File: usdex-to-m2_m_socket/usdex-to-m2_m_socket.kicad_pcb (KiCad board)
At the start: 6 copper layers, 44 x 39.4 mm, 10 parts, among them J1 Conn_02x01, J2 Bus_M.2_Socket_M, J3 Conn_01x02_Pin, J4 Micro_SDex_PCB, J5 Conn_01x02_Pin, J6 Conn_01x02_Pin, J7 Conn_01x10_Pin

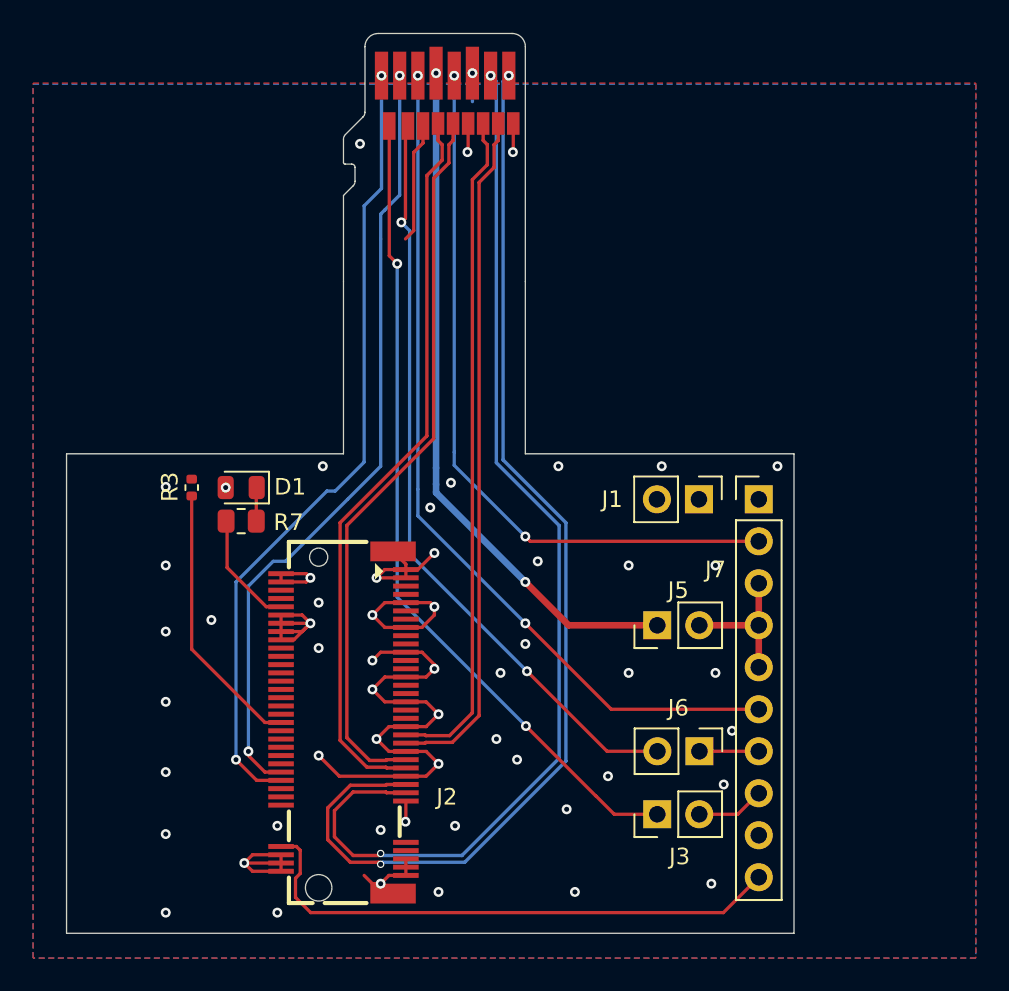
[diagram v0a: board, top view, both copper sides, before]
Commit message: usdex-to-m2_m_socket: fillet tracks
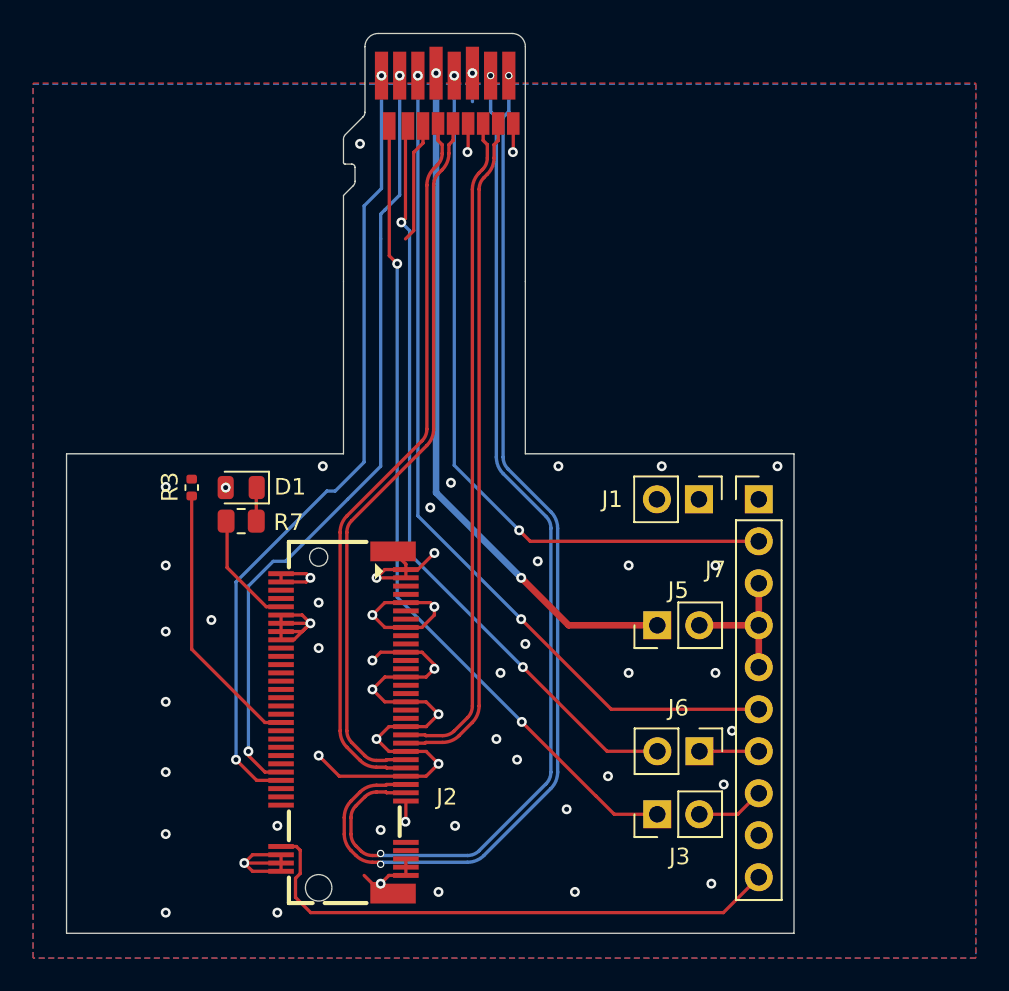
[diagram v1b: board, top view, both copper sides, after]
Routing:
- net DATx/REFCLK-: track 68.0 -> 65.7 mm
- net DATx/REFCLK+: track 66.0 -> 63.8 mm

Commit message: usdex-to-m2_m_socket: tune skew
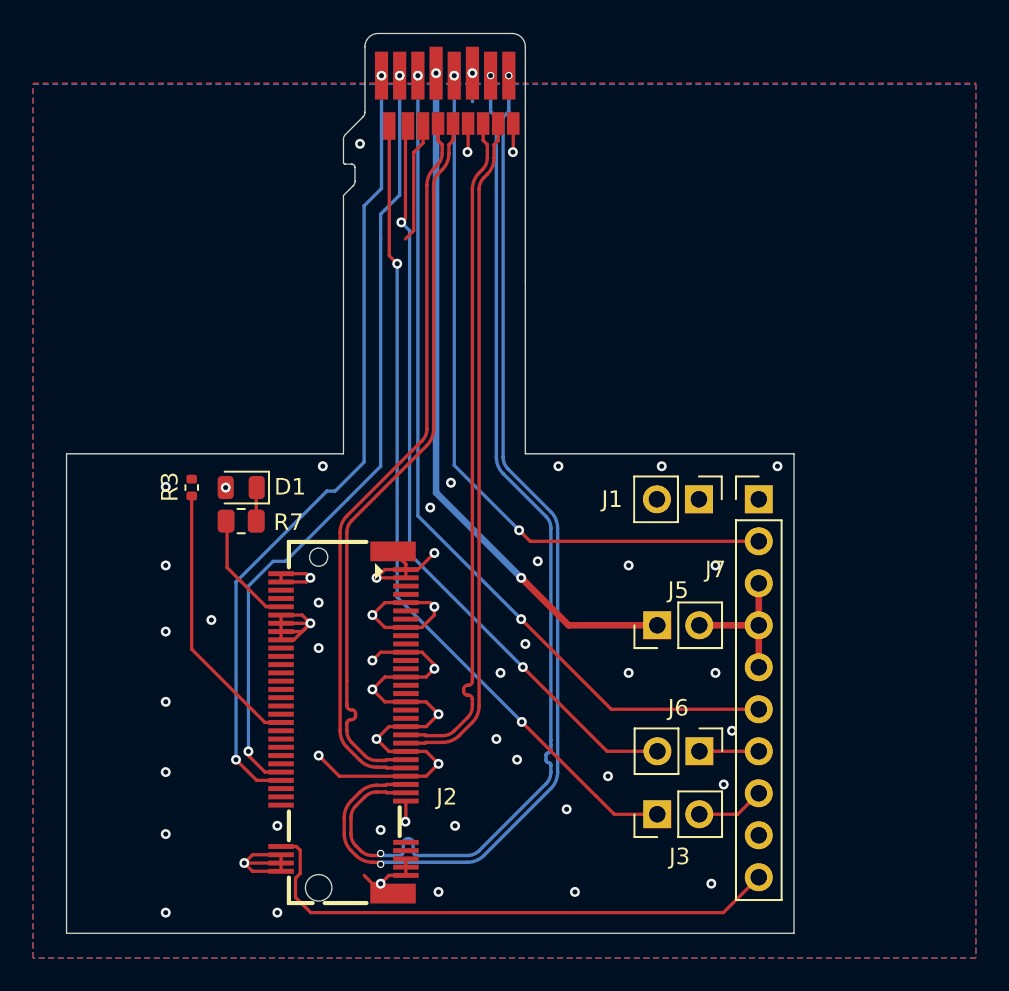
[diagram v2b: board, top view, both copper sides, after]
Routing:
- net DATx/REFCLK+: track 63.8 -> 65.6 mm
- net PCIe_TX-: track 43.6 -> 44.2 mm
- net PCIe_RX-: track 40.5 -> 41.1 mm

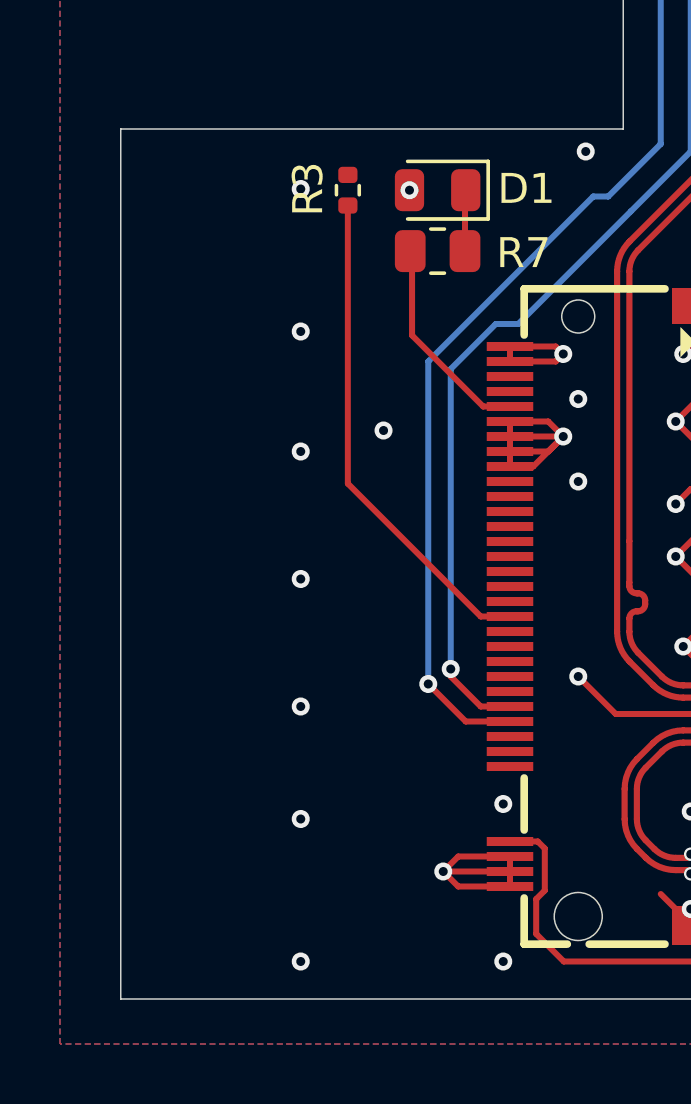
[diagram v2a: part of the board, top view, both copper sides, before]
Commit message: usdex-to-m2_m_socket: move GND vias
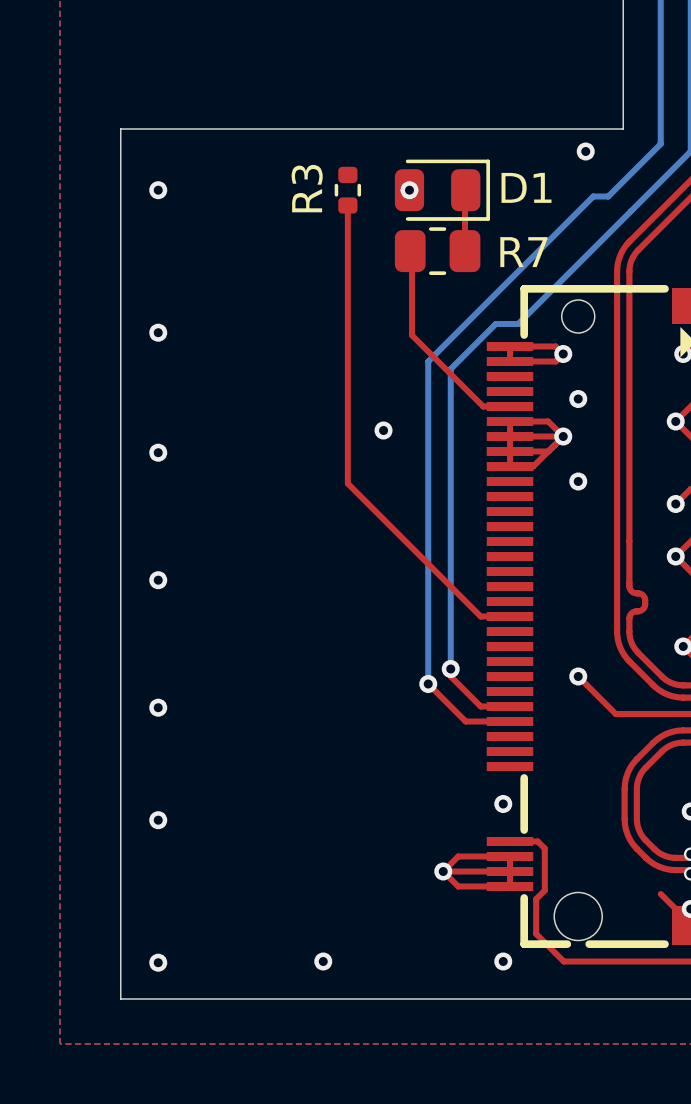
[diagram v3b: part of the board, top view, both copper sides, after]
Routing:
- net GND: vias 53 -> 54
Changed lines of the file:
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@@
 	)
 	(via
-		(at 76 103.25)
+		(at 71.25 103.29)
 		(size 0.6)
 		(drill 0.3)
@@
 	)
 	(via
-		(at 76 90.75)
+		(at 71.25 90.79)
 		(size 0.6)
 		(drill 0.3)
@@
 	)
 	(via
-		(at 76 111.75)
+		(at 71.25 111.79)
 		(size 0.6)
 		(drill 0.3)
@@
 	)
 	(via
+		(at 76.75 111.75)
+		(size 0.6)
+		(drill 0.3)
+		(layers "F.Cu" "B.Cu")
+		(free yes)
+		(net 2)
+	)
+	(via
 		(at 102.75 103.5)
 		(size 0.6)
@@
 	)
 	(via
-		(at 76 94.75)
+		(at 71.25 94.79)
 		(size 0.6)
 		(drill 0.3)
@@
 	)
 	(via
-		(at 76 107)
-		(size 0.6)
-		(drill 0.3)
-		(layers "F.Cu" "B.Cu")
-		(free yes)
-		(net 2)
-	)
-	(via
-		(at 76 99)
+		(at 71.25 107.04)
+		(size 0.6)
+		(drill 0.3)
+		(layers "F.Cu" "B.Cu")
+		(free yes)
+		(net 2)
+	)
+	(via
+		(at 71.25 99.04)
 		(size 0.6)
 		(drill 0.3)
@@
 	)
 	(via
-		(at 76 86)
-		(size 0.6)
-		(drill 0.3)
+		(at 71.25 86.04)
+		(size 0.6)
+		(drill 0.3)
